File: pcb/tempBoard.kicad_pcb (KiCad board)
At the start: 2 copper layers, 31.6 x 62.4 mm, 9 parts, among them J1 OLED_128X64_1.3_I2C, U1 SHTC3, U2 XIAO-RP2040-DIP

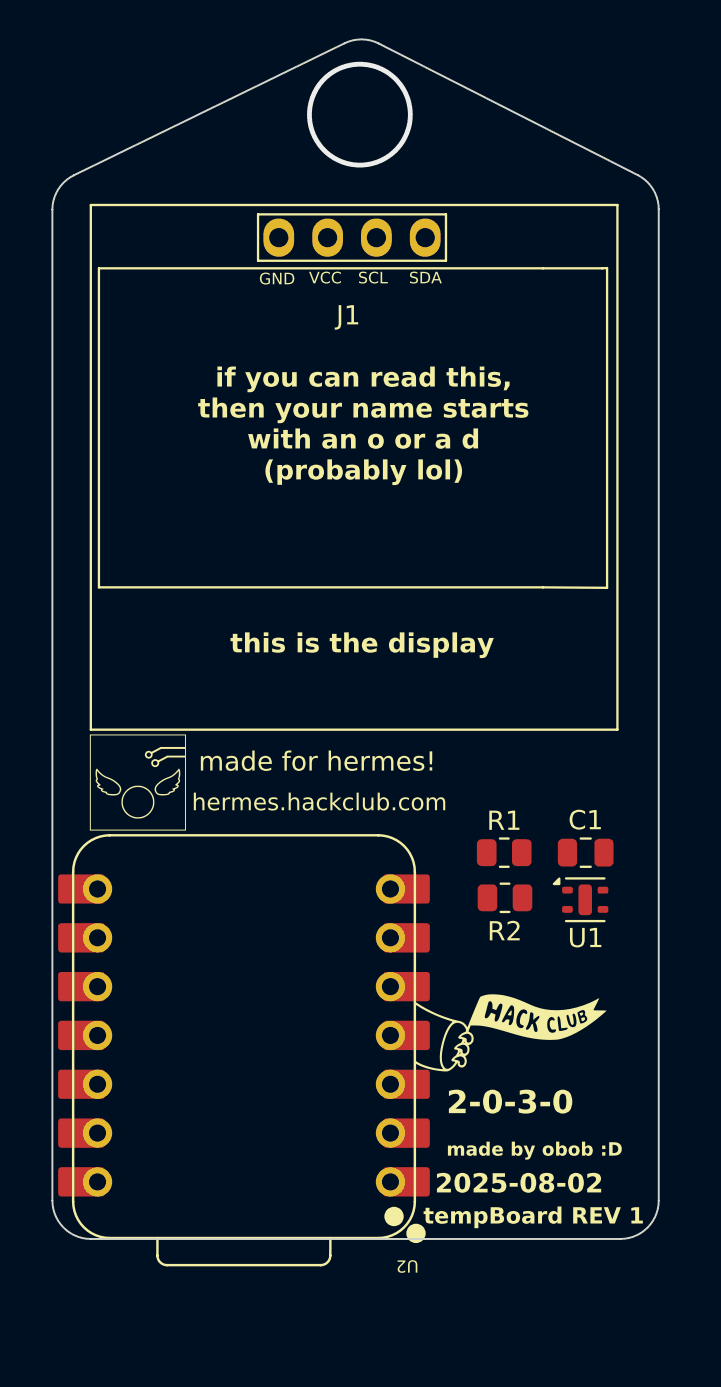
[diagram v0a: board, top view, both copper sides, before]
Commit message: added indicator lights
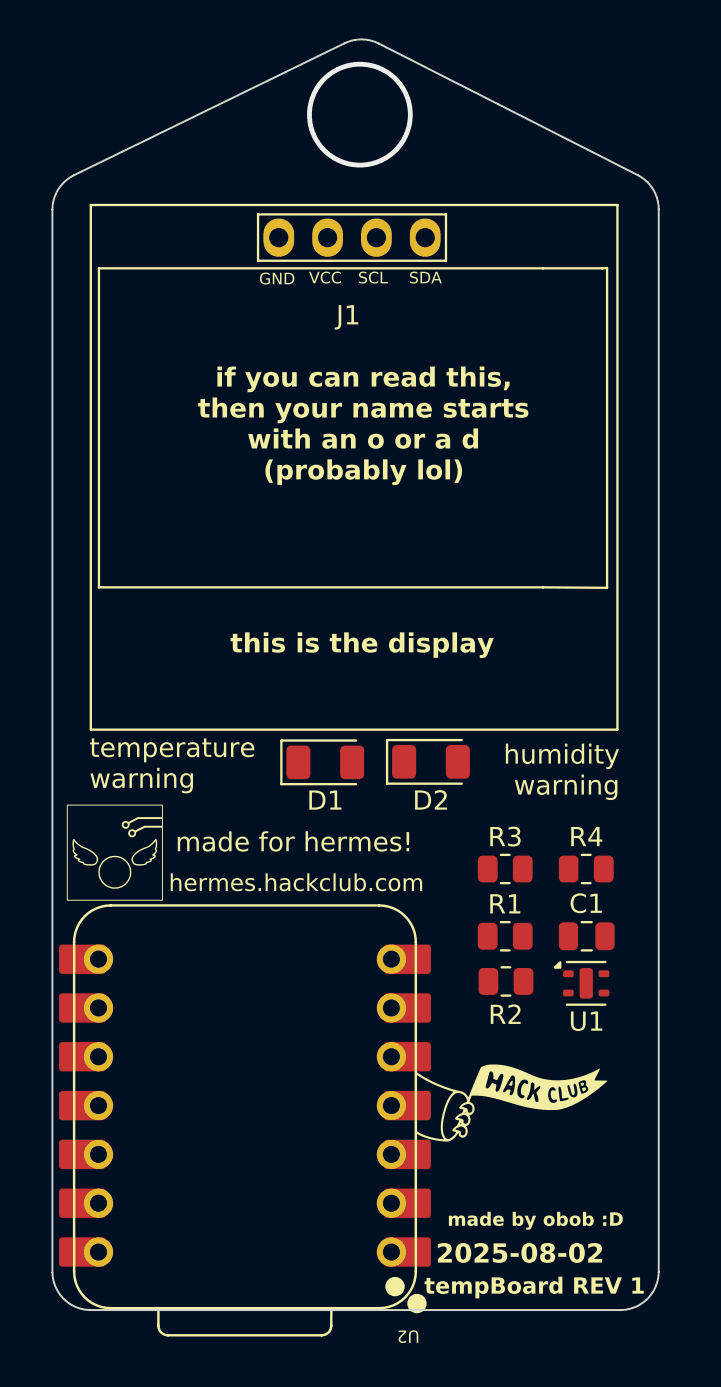
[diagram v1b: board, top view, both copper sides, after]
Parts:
- added D1: LED_RED, LED_SMD:LED_1206_3216Metric, F.Cu at (164.7, 87.2)
- added D2: LED_BLUE, LED_SMD:LED_1206_3216Metric, F.Cu at (170.2, 87.2)
- added R3: 220, Resistor_SMD:R_0805_2012Metric, F.Cu at (174.1, 92.8)
- added R4: 220, Resistor_SMD:R_0805_2012Metric, F.Cu at (178.3, 92.8)
- R1, R2: value R -> 4k7
- moved U1 4.35 mm to (178.3, 98.7)
- moved C1 4.35 mm to (178.3, 96.2)
- moved R1 4.35 mm to (174.1, 96.2)
- moved R2 4.35 mm to (174.1, 98.6)
- moved G*** 3.84 mm to (153.8, 91.9)
- moved G*** 3.65 mm to (174.4, 104.9)
- moved U2 3.65 mm to (160.5, 105.1)
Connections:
- U2 pad 8: unconnected-(U2-GPIO1/RX-Pad8)_1 -> TEMP
- U2 pad 9: unconnected-(U2-GPIO2/SCK-Pad9)_1 -> HUM
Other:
- board size 31.6 x 62.4 mm -> 31.6 x 66.1 mm
- board text added: "NSB 2030"
- board text added: "humidity warning"
- board text added: "temperature warning"
- board text removed: "2-0-3-0"

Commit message: update readme
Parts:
- turned R2 to 180 degrees
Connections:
- U1 pad 5: unconnected-(U1-NC-Pad5) -> GND
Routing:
- net +3V3: track 0.00 -> 97.0 mm
- net SCL: track 0.00 -> 64.4 mm, vias 0 -> 1
- net SDA: track 0.00 -> 63.0 mm
- net GND: track 0.00 -> 31.5 mm, vias 0 -> 3
- net HUM: track 0.00 -> 27.5 mm
- net TEMP: track 0.00 -> 22.2 mm
- net Net-(D1-A): track 0.00 -> 11.2 mm
- net Net-(D2-A): track 0.00 -> 9.90 mm
- added copper zone on B.Cu, net GND
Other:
- board size 31.6 x 66.1 mm -> 33.3 x 66.1 mm

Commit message: remake production files + lcsc part number fields
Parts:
- R3: value 220 -> 68
- R4: value 220 -> 27
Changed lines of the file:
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@@
+			)
+		)
+		(property "LCSC" "C965822"
+			(at 0 0 0)
+			(unlocked yes)
+			(layer "F.Fab")
+			(hide yes)
+			(effects
+				(font
+					(size 1 1)
+					(thickness 0.15)
+				)
 			)
 		)
@@
 		(sheetname "Root")
 		(sheetfile "tempBoard.kicad_sch")
-		(attr through_hole)
+		(attr through_hole exclude_from_pos_files exclude_from_bom dnp)
 		(fp_line
 			(start -13.4 -12.3)
@@
 			)
 		)
+		(property "LCSC" "C28310438"
+			(at 0 0 0)
+			(unlocked yes)
+			(layer "F.Fab")
+			(hide yes)
+			(effects
+				(font
+					(size 1 1)
+					(thickness 0.15)
+				)
+			)
+		)
 		(property ki_fp_filters "LED* LED_SMD:* LED_THT:*")
 		(sheetname "Root")
@@
 				(font
 					(size 1.27 1.27)
+					(thickness 0.15)
+				)
+			)
+		)
+		(property "LCSC" "C49678"
+			(at 0 0 0)
+			(unlocked yes)
+			(layer "F.Fab")
+			(hide yes)
+			(effects
+				(font
+					(size 1 1)
 					(thickness 0.15)
 				)
@@
 		(sheetname "Root")
 		(sheetfile "tempBoard.kicad_sch")
-		(attr smd)
+		(attr smd exclude_from_pos_files exclude_from_bom dnp)
 		(fp_line
 			(start 8.89 8.509)
@@
 			)
 		)
+		(property "LCSC" "C194656"
+			(at 0 0 0)
+			(unlocked yes)
+			(layer "F.Fab")
+			(hide yes)
+			(effects
+				(font
+					(size 1 1)
+					(thickness 0.15)
+				)
+			)
+		)
 		(property ki_fp_filters "Sensirion*DFN*1EP*2x2mm*P1mm*EP0.7x1.6mm*")
 		(sheetname "Root")
@@
 			)
 		)
+		(property "LCSC" "C60816"
+			(at 0 0 0)
+			(unlocked yes)
+			(layer "F.Fab")
+			(hide yes)
+			(effects
+				(font
+					(size 1 1)
+					(thickness 0.15)
+				)
+			)
+		)
 		(property ki_fp_filters "R_*")
 		(sheetname "Root")
@@
 			)
 		)
-		(property "Value" "220"
+		(property "Value" "68"
 			(at 0 1.65 0)
 			(layer "F.Fab")
@@
 				(font
 					(size 1.27 1.27)
+					(thickness 0.15)
+				)
+			)
+		)
+		(property "LCSC" "C17802"
+			(at 0 0 0)
+			(unlocked yes)
+			(layer "F.Fab")
+			(hide yes)
+			(effects
+				(font
+					(size 1 1)
 					(thickness 0.15)
 				)
@@
 			)
 		)
+		(property "LCSC" "C60816"
+			(at 0 0 0)
+			(unlocked yes)
+			(layer "F.Fab")
+			(hide yes)
+			(effects
+				(font
+					(size 1 1)
+					(thickness 0.15)
+				)
+			)
+		)
 		(property ki_fp_filters "R_*")
 		(sheetname "Root")
@@
 			)
 		)
-		(property "Value" "220"
+		(property "Value" "27"
 			(at 0 1.65 0)
 			(layer "F.Fab")
@@
 					(thickness 0.15)
 				)
+			)
+		)
+		(property "LCSC" "C17594"
+			(at 0 0 0)
+			(unlocked yes)
+			(layer "F.Fab")
+			(hide yes)
+			(effects
+				(font
+					(size 1 1)
+					(thickness 0.15)
+				)

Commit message: update production files
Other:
- board text added: "tempBoard REV 2"
- board text added: "tempBoard is a device that measures temperature and humidity and shows it on a screen"
- board text removed: "tempBoard REV 1"
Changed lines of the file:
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@@
 	)
 	(gr_text "this is\na decoupling\ncapactitor,\nit filters out noise"
-		(at 177 87.45 -0)
+		(at 177.75 86.91 -0)
 		(layer "B.SilkS")
 		(effects
@@
 		)
 	)
+	(gr_text "tempBoard is a device\nthat measures temperature\nand humidity and shows\nit on a screen"
+		(at 162.38 93.49 0)
+		(layer "B.SilkS")
+		(effects
+			(font
+				(size 1 1)
+				(thickness 0.2)
+				(bold yes)
+			)
+			(justify bottom mirror)
+		)
+	)
 	(gr_text "self-promotion\n(pls scan)"
 		(at 165.95 83.15 -0)
@@
 		)
 	)
-	(gr_text "tempBoard REV 1"
+	(gr_text "tempBoard REV 2"
 		(at 169.85 114.95 0)
 		(layer "F.SilkS")

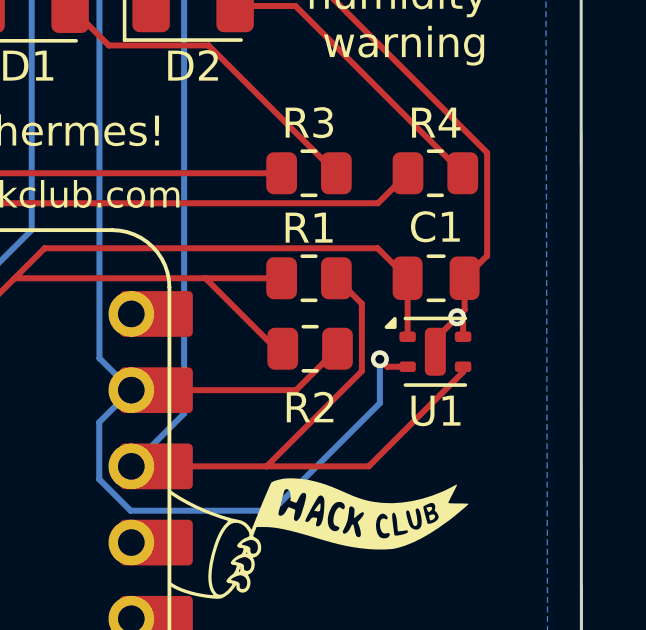
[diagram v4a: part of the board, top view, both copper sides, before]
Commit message: fix some dfm errors
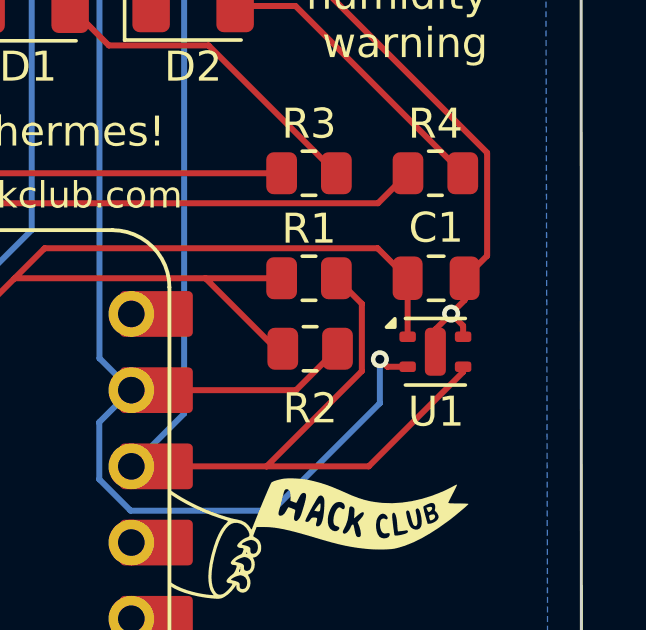
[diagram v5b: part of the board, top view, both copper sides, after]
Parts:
- R4: value 27 -> 33
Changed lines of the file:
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@@
 			)
 		)
-		(property "LCSC" "C60816"
+		(property "LCSC" "C17673"
 			(at 0 0 0)
 			(unlocked yes)
@@
 			)
 		)
-		(property "LCSC" "C60816"
+		(property "LCSC" "C17673"
 			(at 0 0 0)
 			(unlocked yes)
@@
 			)
 		)
-		(property "Value" "27"
+		(property "Value" "33"
 			(at 0 1.65 0)
 			(layer "F.Fab")
@@
 			)
 		)
-		(property "LCSC" "C17594"
+		(property "LCSC" "C17634"
 			(at 0 0 0)
 			(unlocked yes)
@@
 	)
 	(gr_text "the thing with\na hole is the\nsensor itself"
-		(at 176.15 99.8 -0)
+		(at 176.07 106.29 0)
 		(layer "B.SilkS")
 		(effects
@@
 	)
 	(segment
+		(start 178.275 97.955)
+		(end 178.8 97.43)
+		(width 0.2)
+		(layer "F.Cu")
+		(net 1)
+	)
+	(segment
 		(start 163.3 87.2)
 		(end 164.475 86.025)
@@
 	)
 	(segment
-		(start 179.25 96.25)
-		(end 179.25 97.3)
-		(width 0.2)
-		(layer "F.Cu")
-		(net 1)
-	)
-	(segment
 		(start 180 95.5)
 		(end 180 92.065256)
@@
 	)
 	(segment
-		(start 178.275 98.275)
-		(end 179 97.55)
-		(width 0.2)
-		(layer "F.Cu")
-		(net 1)
-	)
-	(segment
-		(start 179.2 98.2)
-		(end 179.2 97.75)
+		(start 179.25 96.98)
+		(end 178.8 97.43)
 		(width 0.2)
 		(layer "F.Cu")
@@
 	)
 	(segment
-		(start 179.25 97.3)
-		(end 179 97.55)
+		(start 179.2 98.2)
+		(end 179.2 97.83)
 		(width 0.2)
 		(layer "F.Cu")
@@
 	(segment
 		(start 178.275 98.7)
-		(end 178.275 98.275)
+		(end 178.275 97.955)
 		(width 0.2)
 		(layer "F.Cu")
@@
 	)
 	(segment
-		(start 179.2 97.75)
-		(end 179 97.55)
+		(start 179.2 97.83)
+		(end 178.8 97.43)
+		(width 0.2)
+		(layer "F.Cu")
+		(net 1)
+	)
+	(segment
+		(start 179.25 96.25)
+		(end 179.25 96.98)
 		(width 0.2)
 		(layer "F.Cu")
@@
 	)
 	(via
-		(at 179 97.55)
+		(at 178.8 97.43)
 		(size 0.6)
 		(drill 0.3)

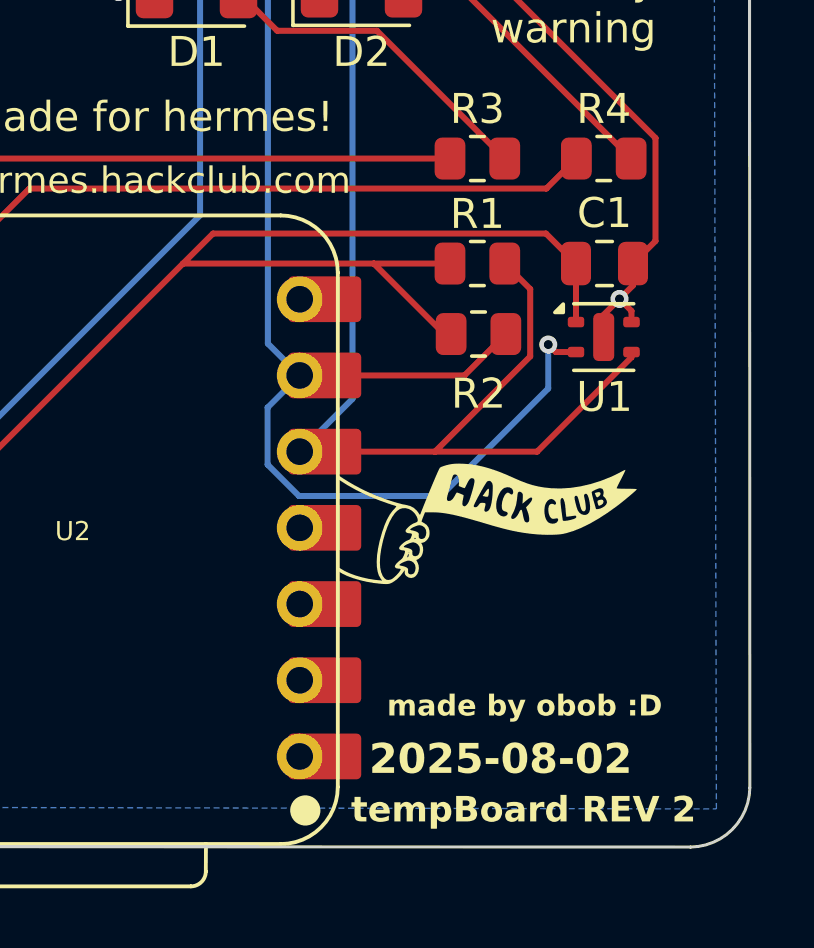
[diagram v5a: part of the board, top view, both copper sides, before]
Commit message: update pullups
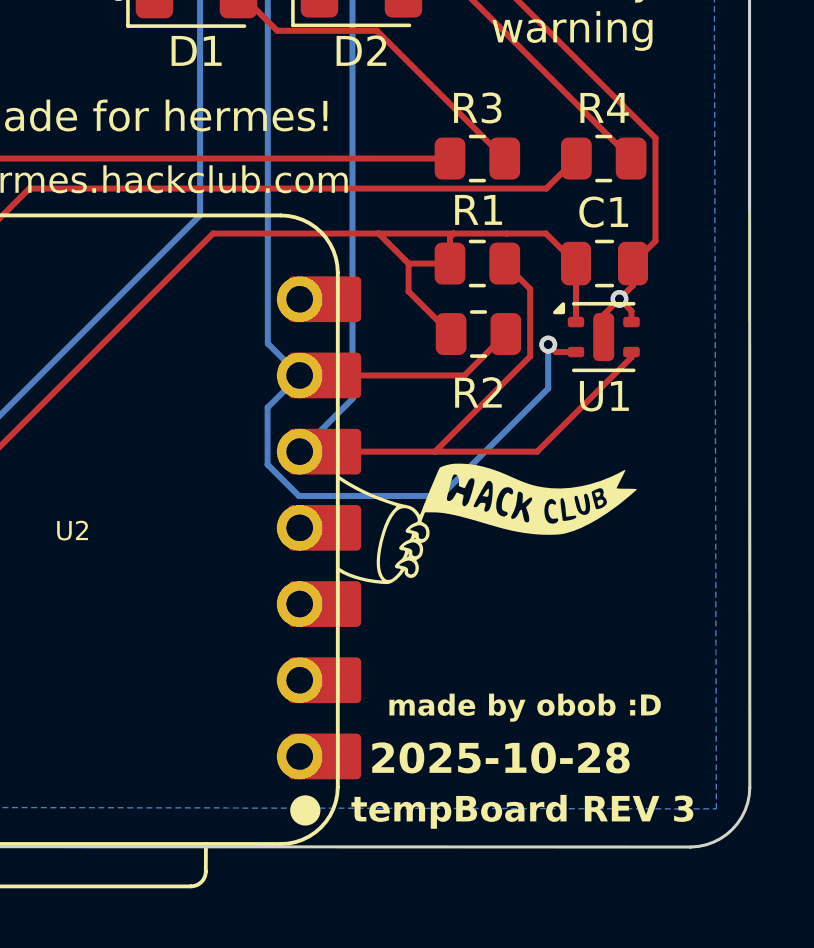
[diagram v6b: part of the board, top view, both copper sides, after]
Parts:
- turned R1 to 180 degrees
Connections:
- R1 pad 1: +3V3 -> SDA
- R1 pad 2: SDA -> +3V3
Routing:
- net +3V3: track 97.0 -> 91.6 mm
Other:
- board text added: "2025-10-28"
- board text added: "tempBoard REV 3"
- board text removed: "2025-08-02"
- board text removed: "tempBoard REV 2"
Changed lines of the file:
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@@
 		(sheetname "Root")
 		(sheetfile "tempBoard.kicad_sch")
-		(attr through_hole exclude_from_pos_files exclude_from_bom dnp)
+		(attr through_hole exclude_from_pos_files)
 		(fp_line
 			(start -13.4 -12.3)
@@
 		(sheetname "Root")
 		(sheetfile "tempBoard.kicad_sch")
-		(attr smd exclude_from_pos_files exclude_from_bom dnp)
+		(attr smd exclude_from_pos_files)
 		(fp_line
 			(start 8.89 8.509)
@@
 	(footprint "Resistor_SMD:R_0805_2012Metric"
 		(layer "F.Cu")
-		(at 174.0625 96.25)
+		(at 174.0625 96.25 180)
 		(descr "Resistor SMD 0805 (2012 Metric), square (rectangular) end terminal, IPC_7351 nominal, (Body size source: IPC-SM-782 page 72, https://www.pcb-3d.com/wordpress/wp-content/uploads/ipc-sm-782a_amendment_1_and_2.pdf), generated with kicad-footprint-generator")
 		(tags "resistor")
 		(property "Reference" "R1"
-			(at 0 -1.65 0)
+			(at -0.0375 1.75 360)
 			(layer "F.SilkS")
 			(effects
@@
 		)
 		(property "Value" "4k7"
-			(at 0 1.65 0)
+			(at 0 1.65 360)
 			(layer "F.Fab")
 			(effects
@@
 		)
 		(property "Footprint" "Resistor_SMD:R_0805_2012Metric"
-			(at 0 0 0)
+			(at 0 0 180)
 			(unlocked yes)
 			(layer "F.Fab")
@@
 		)
 		(property "Datasheet" ""
-			(at 0 0 0)
+			(at 0 0 180)
 			(unlocked yes)
 			(layer "F.Fab")
@@
 		)
 		(property "Description" "Resistor"
-			(at 0 0 0)
+			(at 0 0 180)
 			(unlocked yes)
 			(layer "F.Fab")
@@
 		)
 		(property "LCSC" "C17673"
-			(at 0 0 0)
+			(at 0 0 180)
 			(unlocked yes)
 			(layer "F.Fab")
@@
 		(attr smd)
 		(fp_line
-			(start -0.227064 -0.735)
-			(end 0.227064 -0.735)
+			(start -0.227064 0.735)
+			(end 0.227064 0.735)
 			(stroke
 				(width 0.12)
@@
 		)
 		(fp_line
-			(start -0.227064 0.735)
-			(end 0.227064 0.735)
+			(start -0.227064 -0.735)
+			(end 0.227064 -0.735)
 			(stroke
 				(width 0.12)
@@
 		)
 		(fp_line
-			(start -1.68 -0.95)
-			(end 1.68 -0.95)
+			(start 1.68 0.95)
+			(end -1.68 0.95)
 			(stroke
 				(width 0.05)
@@
 		)
 		(fp_line
-			(start -1.68 0.95)
-			(end -1.68 -0.95)
+			(start 1.68 -0.95)
+			(end 1.68 0.95)
 			(stroke
 				(width 0.05)
@@
 		)
 		(fp_line
-			(start 1.68 -0.95)
-			(end 1.68 0.95)
+			(start -1.68 0.95)
+			(end -1.68 -0.95)
 			(stroke
 				(width 0.05)
@@
 		)
 		(fp_line
-			(start 1.68 0.95)
-			(end -1.68 0.95)
+			(start -1.68 -0.95)
+			(end 1.68 -0.95)
 			(stroke
 				(width 0.05)
@@
 		)
 		(fp_line
-			(start -1 -0.625)
-			(end 1 -0.625)
+			(start 1 0.625)
+			(end -1 0.625)
 			(stroke
 				(width 0.1)
@@
 		)
 		(fp_line
-			(start -1 0.625)
-			(end -1 -0.625)
+			(start 1 -0.625)
+			(end 1 0.625)
 			(stroke
 				(width 0.1)
@@
 		)
 		(fp_line
-			(start 1 -0.625)
-			(end 1 0.625)
+			(start -1 0.625)
+			(end -1 -0.625)
 			(stroke
 				(width 0.1)
@@
 		)
 		(fp_line
-			(start 1 0.625)
-			(end -1 0.625)
+			(start -1 -0.625)
+			(end 1 -0.625)
 			(stroke
 				(width 0.1)
@@
 		)
 		(fp_text user "${REFERENCE}"
-			(at 0 0 0)
+			(at 0 0 360)
 			(layer "F.Fab")
 			(effects
@@
 		)
 		(pad "1" smd roundrect
-			(at -0.9125 0)
+			(at -0.9125 0 180)
 			(size 1.025 1.4)
 			(layers "F.Cu" "F.Paste" "F.Mask")
 			(roundrect_rratio 0.243902)
-			(net 2 "+3V3")
+			(net 4 "SDA")
 			(pintype "passive")
 		)
 		(pad "2" smd roundrect
-			(at 0.9125 0)
+			(at 0.9125 0 180)
 			(size 1.025 1.4)
 			(layers "F.Cu" "F.Paste" "F.Mask")
 			(roundrect_rratio 0.243902)
-			(net 4 "SDA")
+			(net 2 "+3V3")
 			(pintype "passive")
 		)
@@
 		)
 	)
-	(gr_text "tempBoard REV 2"
+	(gr_text "tempBoard REV 3"
 		(at 169.85 114.95 0)
 		(layer "F.SilkS")
@@
 		)
 	)
-	(gr_text "2025-08-02"
+	(gr_text "2025-10-28"
 		(at 170.45 113.35 0)
 		(layer "F.SilkS")
@@
 	)
 	(segment
-		(start 170.61 96.25)
-		(end 164.25 96.25)
+		(start 175.04 95.25)
+		(end 173.27 95.25)
+		(width 0.2)
+		(layer "F.Cu")
+		(net 2)
+	)
+	(segment
+		(start 171.77 97.1825)
+		(end 173.1875 98.6)
+		(width 0.2)
+		(layer "F.Cu")
+		(net 2)
+	)
+	(segment
+		(start 173.27 95.25)
+		(end 170.77 95.25)
+		(width 0.2)
+		(layer "F.Cu")
+		(net 2)
+	)
+	(segment
+		(start 173.27 95.25)
+		(end 173.15 95.37)
+		(width 0.2)
+		(layer "F.Cu")
+		(net 2)
+	)
+	(segment
+		(start 173.22 98.5675)
+		(end 173.1875 98.6)
+		(width 0.2)
+		(layer "F.Cu")
+		(net 2)
+	)
+	(segment
+		(start 171.77 96.25)
+		(end 171.77 97.1825)
+		(width 0.2)
+		(layer "F.Cu")
+		(net 2)
+	)
+	(segment
+		(start 171.77 96.25)
+		(end 173.15 96.25)
 		(width 0.2)
 		(layer "F.Cu")
@@
 	)
 	(segment
-		(start 172.96 98.6)
-		(end 170.61 96.25)
+		(start 170.77 95.25)
+		(end 165.25 95.25)
 		(width 0.2)
 		(layer "F.Cu")
@@
 	)
 	(segment
+		(start 171.645 96.125)
+		(end 171.77 96.25)
+		(width 0.2)
+		(layer "F.Cu")
+		(net 2)
+	)
+	(segment
 		(start 177.35 96.25)
 		(end 176.35 95.25)
@@
 	)
 	(segment
-		(start 176.35 95.25)
-		(end 165.25 95.25)
+		(start 170.77 95.25)
+		(end 171.645 96.125)
 		(width 0.2)
 		(layer "F.Cu")
@@
 	)
 	(segment
+		(start 173.15 95.37)
+		(end 173.15 96.25)
+		(width 0.2)
+		(layer "F.Cu")
+		(net 2)
+	)
+	(segment
 		(start 164.25 96.25)
 		(end 152.9 107.6)
@@
 	)
 	(segment
-		(start 173.15 96.25)
-		(end 170.61 96.25)
+		(start 176.35 95.25)
+		(end 175.04 95.25)
 		(width 0.2)
 		(layer "F.Cu")
@@
 		(width 0.2)
 		(layer "F.Cu")
+		(net 4)
+	)
+	(segment
+		(start 175.04 95.85)
+		(end 174.975 95.85)
+		(width 0.2)
+		(layer "F.Cu")
